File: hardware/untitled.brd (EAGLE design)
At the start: 68.6 x 47.9 mm, 44 parts, among them IC2 LM1117IMPX-3.3, U4 microSD, Y1 CRYSTAL-GROUNDEDSMD-5X3.2

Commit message: Reset fix
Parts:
- added C17: 100n, rcl:C0603
- added R12: (no value), rcl:R0603
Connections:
- net 3V: now also R12.2
- net GND: now also C17.2
- net NRST: now also C17.1, R12.1
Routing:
- net NRST: track 21.9 -> 23.4 mm
- net 3V: track 184.0 -> 185.5 mm
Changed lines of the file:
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@@
 <element name="C11" library="rcl" package="C0603" value="" x="49.9364" y="11.6062" rot="MR0"/>
 <element name="C16" library="rcl" package="SMC_B" value="" x="55.8546" y="11.6062"/>
+<element name="R12" library="rcl" package="R0603" value="" x="29.21" y="16.7386" rot="MR90"/>
+<element name="C17" library="rcl" package="C0603" value="100n" x="29.21" y="13.5636" rot="MR270"/>
 </elements>
 <signals>
@@
 <contactref element="C16" pad="-"/>
 <via x="56.5658" y="20.066" extent="1-16" drill="0.6" diameter="1.4224" shape="octagon"/>
+<contactref element="C17" pad="2"/>
 </signal>
 <signal name="PE1">
@@
 <via x="52.3764" y="11.6062" extent="1-16" drill="0.6" diameter="1.4224" shape="octagon"/>
 <wire x1="52.3764" y1="11.6062" x2="54.3546" y2="11.6062" width="1.016" layer="1"/>
+<contactref element="R12" pad="2"/>
+<wire x1="29.21" y1="17.5886" x2="29.21" y2="19.05" width="0.6096" layer="16"/>
 </signal>
 <signal name="5V">
@@
 <wire x1="26.8874" y1="16.4226" x2="26.3398" y2="15.875" width="0.3048" layer="1"/>
 <via x="26.3398" y="15.875" extent="1-16" drill="0.6" diameter="1.4224" shape="octagon"/>
-<wire x1="26.3398" y1="15.875" x2="36.195" y2="15.875" width="0.4064" layer="16"/>
+<wire x1="26.3398" y1="15.875" x2="29.21" y2="15.875" width="0.4064" layer="16"/>
+<wire x1="29.21" y1="15.875" x2="36.195" y2="15.875" width="0.4064" layer="16"/>
 <wire x1="36.195" y1="15.875" x2="40.64" y2="20.32" width="0.4064" layer="16"/>
 <wire x1="44.3992" y1="20.32" x2="40.64" y2="20.32" width="0.4064" layer="16"/>
+<contactref element="R12" pad="1"/>
+<contactref element="C17" pad="1"/>
+<wire x1="29.21" y1="15.8886" x2="29.21" y2="15.875" width="0.4064" layer="16"/>
+<wire x1="29.21" y1="14.4136" x2="29.21" y2="15.8886" width="0.6096" layer="16"/>
 </signal>
 <signal name="SWD_CLK">

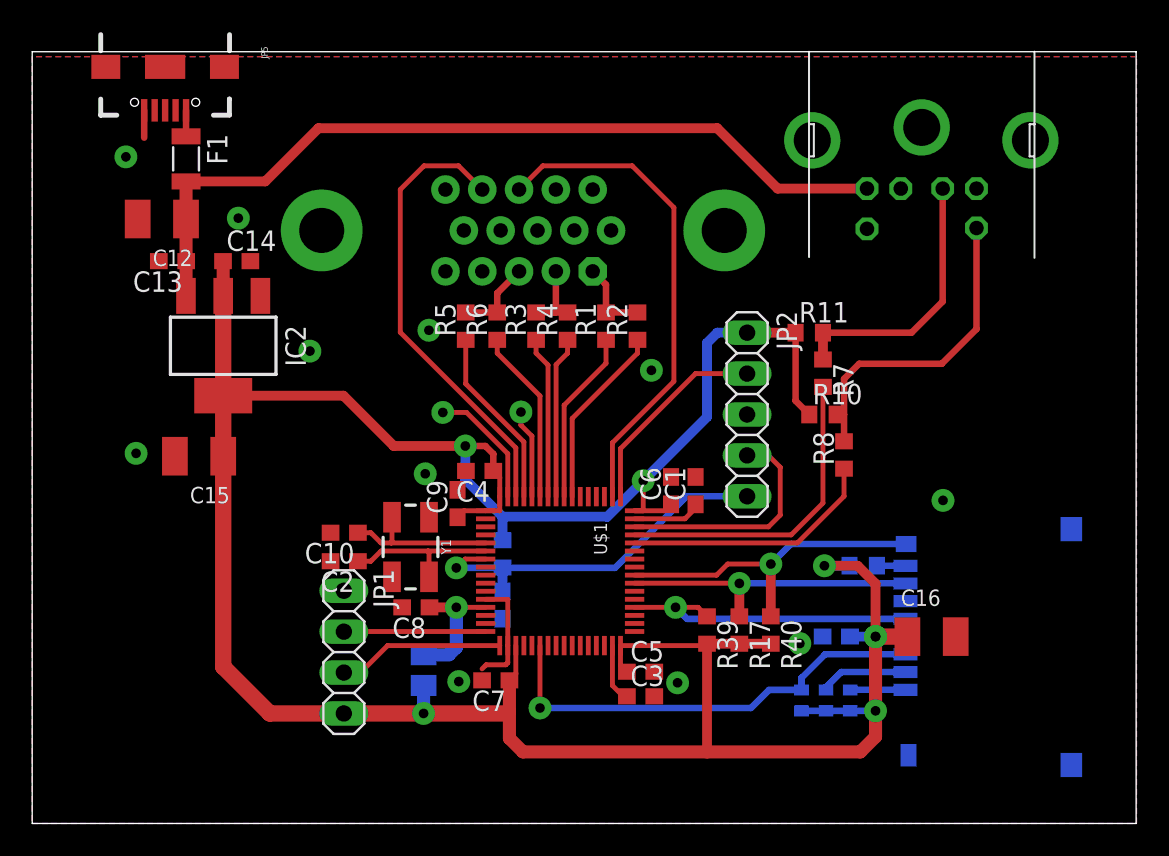
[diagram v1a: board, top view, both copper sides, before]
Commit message: More GND vias
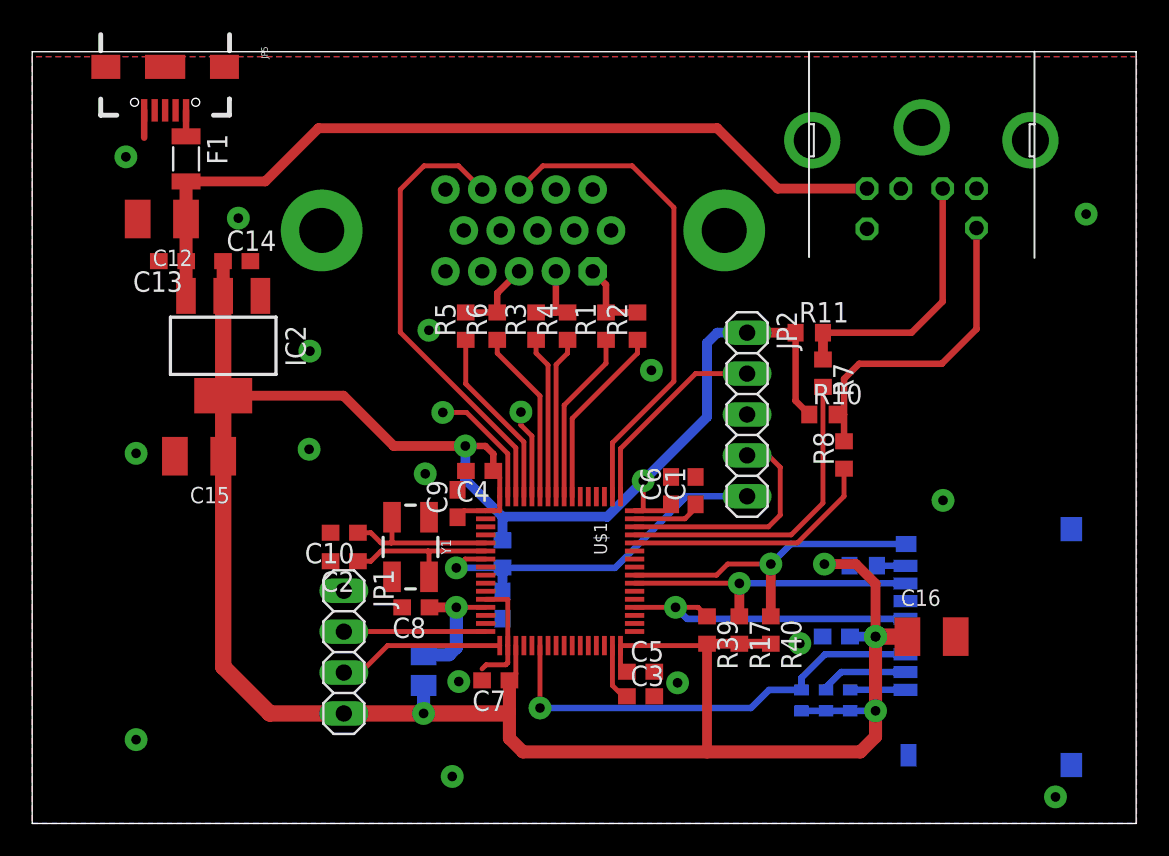
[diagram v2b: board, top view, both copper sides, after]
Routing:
- net GND: vias 13 -> 18
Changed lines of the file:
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@@
 <via x="56.5658" y="20.066" extent="1-16" drill="0.6" diameter="1.4224" shape="octagon"/>
 <contactref element="C17" pad="2"/>
+<via x="6.4516" y="5.207" extent="1-16" drill="0.6" diameter="1.4224" shape="octagon"/>
+<via x="65.4558" y="37.846" extent="1-16" drill="0.6" diameter="1.4224" shape="octagon"/>
+<via x="63.5508" y="1.651" extent="1-16" drill="0.6" diameter="1.4224" shape="octagon"/>
+<via x="17.1958" y="23.241" extent="1-16" drill="0.6" diameter="1.4224" shape="octagon"/>
+<via x="26.0858" y="2.921" extent="1-16" drill="0.6" diameter="1.4224" shape="octagon"/>
 </signal>
 <signal name="PE1">
@@
 <wire x1="51.435" y1="4.445" x2="52.3748" y2="5.3848" width="0.8128" layer="1"/>
 <wire x1="52.3748" y1="6.9954" x2="52.3748" y2="5.3848" width="0.8128" layer="1"/>
-<via x="49.1998" y="16.0062" extent="1-16" drill="0.6" diameter="1.4224" shape="octagon"/>
+<via x="49.1998" y="16.1078" extent="1-16" drill="0.6" diameter="1.4224" shape="octagon"/>
 <wire x1="36.5362" y1="11.0476" x2="41.7934" y2="11.0476" width="0.3048" layer="1"/>
 <wire x1="41.91" y1="11.1642" x2="41.91" y2="4.445" width="0.6096" layer="1"/>
 <wire x1="41.7934" y1="11.0476" x2="41.91" y2="11.1642" width="0.3048" layer="1"/>
-<wire x1="49.1998" y1="16.0062" x2="50.7628" y2="16.0062" width="0.6096" layer="16"/>
-<wire x1="49.1998" y1="16.0062" x2="51.2648" y2="16.0062" width="0.6096" layer="1"/>
-<wire x1="51.2648" y1="16.0062" x2="52.3748" y2="14.8962" width="0.6096" layer="1"/>
+<wire x1="51.1632" y1="16.1078" x2="52.3748" y2="14.8962" width="0.6096" layer="1"/>
 <wire x1="41.91" y1="11.1642" x2="43.9166" y2="11.1642" width="0.6096" layer="1"/>
 <wire x1="43.9166" y1="11.1642" x2="45.8724" y2="11.1642" width="0.6096" layer="1"/>
@@
 <contactref element="R12" pad="2"/>
 <wire x1="29.21" y1="17.5886" x2="29.21" y2="19.05" width="0.6096" layer="16"/>
+<wire x1="49.1998" y1="16.1078" x2="50.6612" y2="16.1078" width="0.6096" layer="16"/>
+<wire x1="50.6612" y1="16.1078" x2="50.7628" y2="16.0062" width="0.6096" layer="16"/>
+<wire x1="49.1998" y1="16.1078" x2="51.1632" y2="16.1078" width="0.6096" layer="1"/>
 </signal>
 <signal name="5V">

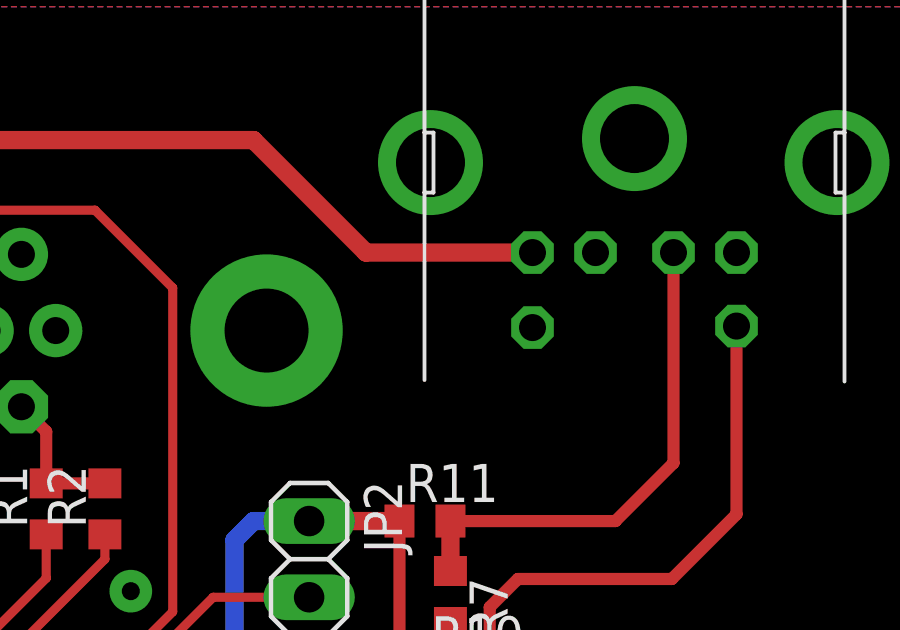
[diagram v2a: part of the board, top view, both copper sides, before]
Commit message: Capacitor at PS/2 socket
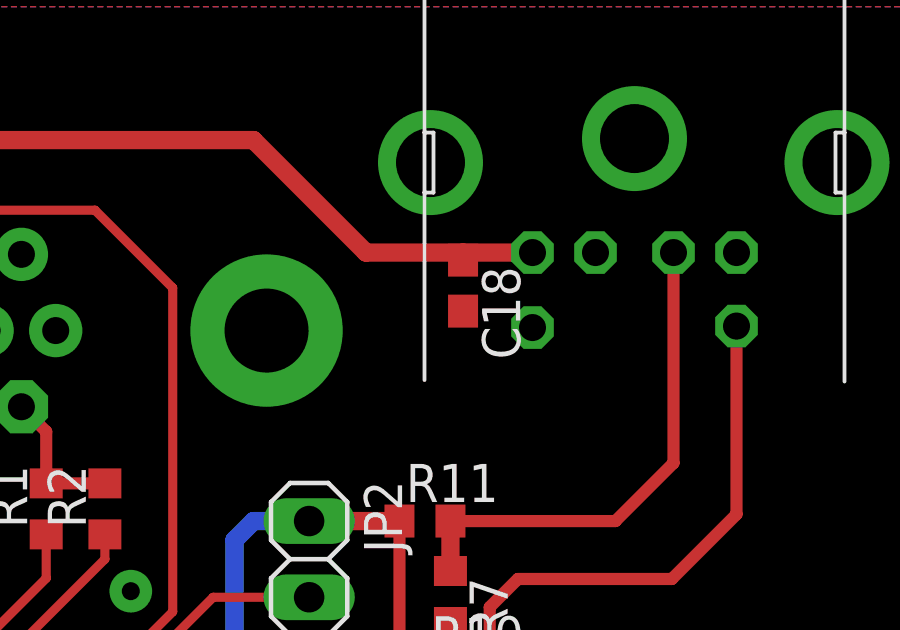
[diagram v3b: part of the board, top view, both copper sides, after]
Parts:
- added C18: (no value), rcl:C0603
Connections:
- net 5V: now also C18.1
- net GND: now also C18.2
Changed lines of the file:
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@@
 <element name="R12" library="rcl" package="R0603" value="" x="29.21" y="16.7386" rot="MR90"/>
 <element name="C17" library="rcl" package="C0603" value="100n" x="29.21" y="13.5636" rot="MR270"/>
+<element name="C18" library="rcl" package="C0603" value="" x="49.53" y="38.3286" rot="R270"/>
 </elements>
 <signals>
@@
 <via x="17.1958" y="23.241" extent="1-16" drill="0.6" diameter="1.4224" shape="octagon"/>
 <via x="26.0858" y="2.921" extent="1-16" drill="0.6" diameter="1.4224" shape="octagon"/>
+<contactref element="C18" pad="2"/>
 </signal>
 <signal name="PE1">
@@
 <wire x1="42.545" y1="43.18" x2="46.295" y2="39.43" width="0.6096" layer="1"/>
 <contactref element="X2" pad="5"/>
-<wire x1="51.845" y1="39.43" x2="46.295" y2="39.43" width="0.6096" layer="1"/>
+<wire x1="51.845" y1="39.43" x2="49.53" y2="39.43" width="0.6096" layer="1"/>
+<contactref element="C18" pad="1"/>
+<wire x1="49.53" y1="39.43" x2="46.295" y2="39.43" width="0.6096" layer="1"/>
+<wire x1="49.53" y1="39.1786" x2="49.53" y2="39.43" width="0.4064" layer="1"/>
 </signal>
 <signal name="NRST">
